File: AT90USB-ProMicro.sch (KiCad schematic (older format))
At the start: 20 parts, among them J1 Conn_01x12, J2 Conn_01x12, J3 Conn_01x03, U1 AT90USB162-16MU, U2 SOT-23 3.3V, X1 8MHz 2520

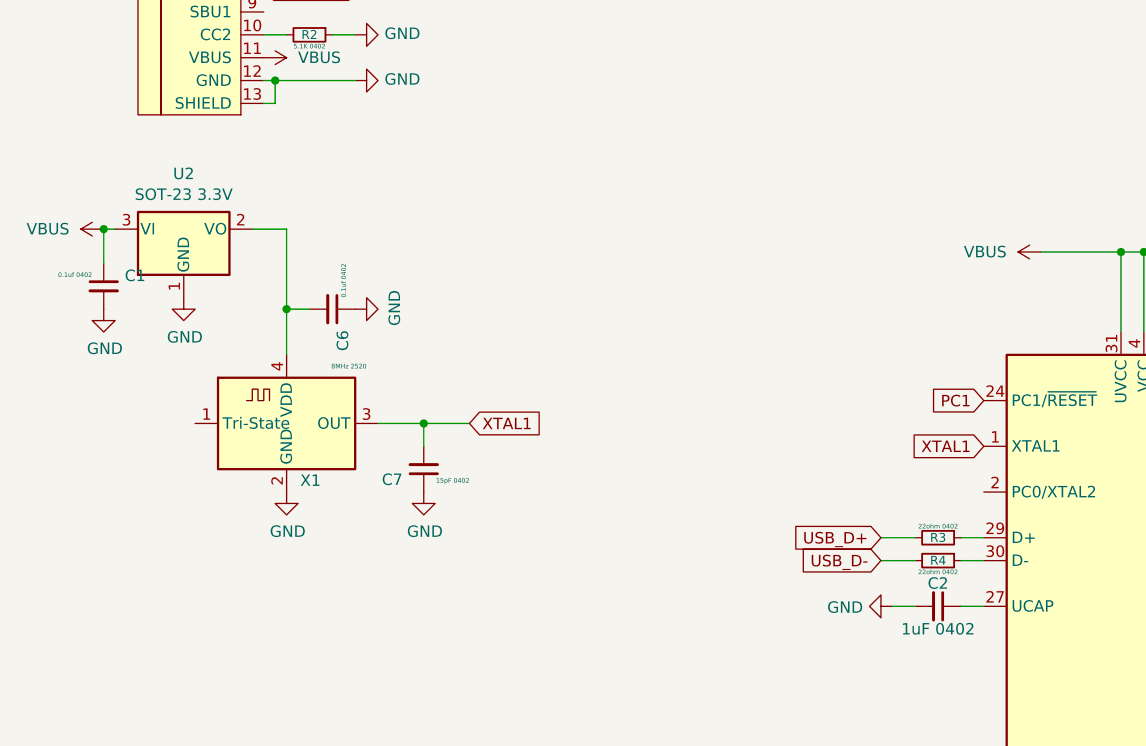
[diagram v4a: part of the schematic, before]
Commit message: changed oscillator for crystal, 3225 gnd on 2 and 4.
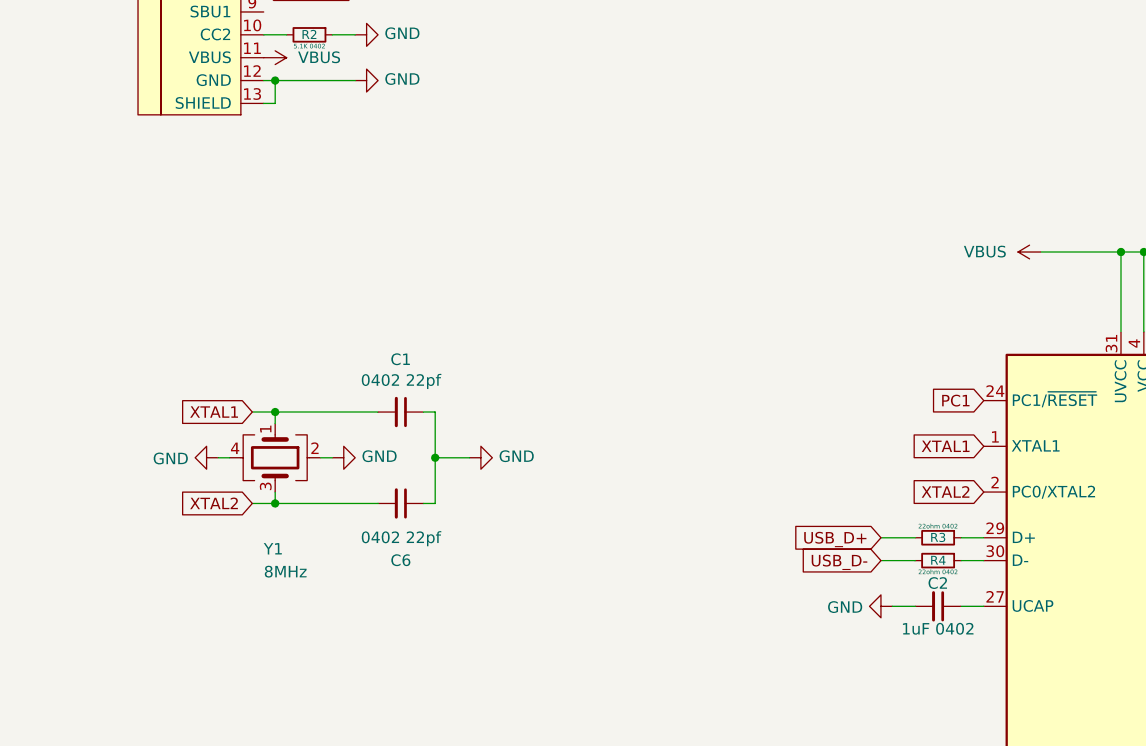
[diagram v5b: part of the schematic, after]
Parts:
- removed C7: 15pF 0402, Capacitor_SMD:C_0402_1005Metric, symbol Device:C_Small
- removed U2: SOT-23 3.3V, Package_TO_SOT_SMD:SOT-23, symbol Regulator_Linear:MCP1703A-3302_SOT23
- removed X1: 8MHz 2520, Oscillator:Oscillator_SMD_ECS_2520MV-xxx-xx-4Pin_2.5x2.0mm, symbol Oscillator:ECS-2520MV-xxx-xx
- added Y1: 8MHz, Crystal:Crystal_SMD_3225-4Pin_3.2x2.5mm, symbol Device:Crystal_GND24
- C1, C6: value 0.1uf 0402 -> 0402 22pf
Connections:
- net GND: now also C1.1, Y1.2, Y1.4; no longer C1.2
- net VBUS: no longer C1.1
- net XTAL1: now also C1.2, Y1.1
- net XTAL2: now reaches U1.2 (PC0/XTAL2)
- net XTAL2: now also C6.2, Y1.3
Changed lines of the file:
@@
 Wire Wire Line
 	4350 5100 4500 5100
-$Comp
-L power:VBUS #PWR0110
-U 1 1 610BDD5E
-P 950 3650
-F 0 "#PWR0110" H 950 3500 50  0001 C CNN
-F 1 "VBUS" V 950 3800 50  0000 L CNN
-F 2 "" H 950 3650 50  0001 C CNN
-F 3 "" H 950 3650 50  0001 C CNN
-	1    950  3650
-	0    -1   -1   0
-$EndComp
 Text GLabel 4800 4600 0    50   Input ~ 0
 XTAL1
-Text GLabel 2550 4500 2    50   Input ~ 0
-XTAL1
-$Comp
-L Device:C_Small C1
-U 1 1 610B5A05
-P 950 3900
-F 0 "C1" H 1042 3946 50  0000 L CNN
-F 1 "0.1uf 0402" H 750 3950 20  0000 L CNN
-F 2 "Capacitor_SMD:C_0402_1005Metric" H 950 3900 50  0001 C CNN
-F 3 "~" H 950 3900 50  0001 C CNN
-	1    950  3900
-	1    0    0    -1
-$EndComp
-Wire Wire Line
-	950  3800 950  3650
-$Comp
-L power:GND #PWR0112
-U 1 1 610B6B7D
-P 950 4000
-F 0 "#PWR0112" H 950 3750 50  0001 C CNN
-F 1 "GND" H 955 3827 50  0000 C CNN
-F 2 "" H 950 4000 50  0001 C CNN
-F 3 "" H 950 4000 50  0001 C CNN
-	1    950  4000
-	1    0    0    -1
-$EndComp
 $Comp
 L Connector_Generic:Conn_01x12 J1
@@
 Connection ~ 5500 6950
 $Comp
-L Oscillator:ECS-2520MV-xxx-xx X1
-U 1 1 611038B7
-P 1750 4500
-F 0 "X1" H 1900 4250 50  0000 R CNN
-F 1 "8MHz 2520" H 2100 4750 20  0000 R CNN
-F 2 "Oscillator:Oscillator_SMD_ECS_2520MV-xxx-xx-4Pin_2.5x2.0mm" H 2200 4150 50  0001 C CNN
-F 3 "https://www.ecsxtal.com/store/pdf/ECS-2520MV.pdf" H 1575 4625 50  0001 C CNN
-	1    1750 4500
-	1    0    0    -1
-$EndComp
-Wire Wire Line
-	950  3650 1000 3650
-Connection ~ 950  3650
-$Comp
-L power:GND #PWR0111
-U 1 1 610BE5C3
-P 1750 4800
-F 0 "#PWR0111" H 1750 4550 50  0001 C CNN
-F 1 "GND" H 1755 4627 50  0000 C CNN
-F 2 "" H 1750 4800 50  0001 C CNN
-F 3 "" H 1750 4800 50  0001 C CNN
-	1    1750 4800
-	1    0    0    -1
-$EndComp
-$Comp
-L power:GND #PWR0114
-U 1 1 61113D49
-P 1300 3950
-F 0 "#PWR0114" H 1300 3700 50  0001 C CNN
-F 1 "GND" H 1305 3777 50  0000 C CNN
-F 2 "" H 1300 3950 50  0001 C CNN
-F 3 "" H 1300 3950 50  0001 C CNN
-	1    1300 3950
-	1    0    0    -1
-$EndComp
-$Comp
-L Regulator_Linear:MCP1703A-3302_SOT23 U2
-U 1 1 611160A9
-P 1300 3650
-F 0 "U2" H 1300 3892 50  0000 C CNN
-F 1 "SOT-23 3.3V" H 1300 3801 50  0000 C CNN
-F 2 "Package_TO_SOT_SMD:SOT-23" H 1300 3850 50  0001 C CNN
-F 3 "http://ww1.microchip.com/downloads/en/DeviceDoc/20005122B.pdf" H 1300 3600 50  0001 C CNN
-	1    1300 3650
-	1    0    0    -1
-$EndComp
-$Comp
 L power:GND #PWR0113
 U 1 1 61140B20
@@
 	0    1    1    0
 $EndComp
-Wire Wire Line
-	1750 4200 1750 4000
-Wire Wire Line
-	1750 3650 1600 3650
+Text GLabel 4800 4800 0    50   Input ~ 0
+XTAL2
+Text GLabel 1600 4850 0    50   Input ~ 0
+XTAL2
+$Comp
+L Device:C_Small C1
+U 1 1 611B395D
+P 2250 4450
+F 0 "C1" V 2021 4450 50  0000 C CNN
+F 1 "0402 22pf" V 2112 4450 50  0000 C CNN
+F 2 "Capacitor_SMD:C_0402_1005Metric" H 2250 4450 50  0001 C CNN
+F 3 "~" H 2250 4450 50  0001 C CNN
+	1    2250 4450
+	0    1    1    0
+$EndComp
 $Comp
 L Device:C_Small C6
-U 1 1 610DB8B7
-P 1950 4000
-F 0 "C6" H 2042 4046 50  0000 L CNN
-F 1 "0.1uf 0402" H 1750 4050 20  0000 L CNN
-F 2 "Capacitor_SMD:C_0402_1005Metric" H 1950 4000 50  0001 C CNN
-F 3 "~" H 1950 4000 50  0001 C CNN
-	1    1950 4000
+U 1 1 611B5404
+P 2250 4850
+F 0 "C6" V 2500 4850 50  0000 C CNN
+F 1 "0402 22pf" V 2400 4850 50  0000 C CNN
+F 2 "Capacitor_SMD:C_0402_1005Metric" H 2250 4850 50  0001 C CNN
+F 3 "~" H 2250 4850 50  0001 C CNN
+	1    2250 4850
 	0    1    1    0
 $EndComp
 $Comp
 L power:GND #PWR02
-U 1 1 610DC063
-P 2050 4000
-F 0 "#PWR02" H 2050 3750 50  0001 C CNN
-F 1 "GND" H 2055 3827 50  0000 C CNN
-F 2 "" H 2050 4000 50  0001 C CNN
-F 3 "" H 2050 4000 50  0001 C CNN
-	1    2050 4000
-	0    -1   -1   0
-$EndComp
-Wire Wire Line
-	1850 4000 1750 4000
-Connection ~ 1750 4000
-Wire Wire Line
-	1750 4000 1750 3650
-$Comp
-L Device:C_Small C7
-U 1 1 610DF85F
-P 2350 4700
-F 0 "C7" H 2442 4746 50  0000 L CNN
-F 1 "15pF 0402" H 2150 4750 20  0000 L CNN
-F 2 "Capacitor_SMD:C_0402_1005Metric" H 2350 4700 50  0001 C CNN
-F 3 "~" H 2350 4700 50  0001 C CNN
-	1    2350 4700
-	-1   0    0    1
-$EndComp
-$Comp
-L power:GND #PWR03
-U 1 1 610DFF21
-P 2350 4800
-F 0 "#PWR03" H 2350 4550 50  0001 C CNN
-F 1 "GND" H 2355 4627 50  0000 C CNN
-F 2 "" H 2350 4800 50  0001 C CNN
-F 3 "" H 2350 4800 50  0001 C CNN
-	1    2350 4800
-	1    0    0    -1
-$EndComp
-Wire Wire Line
-	2150 4500 2350 4500
-Connection ~ 2350 4500
-Wire Wire Line
-	2350 4500 2550 4500
-Wire Wire Line
-	2350 4500 2350 4600
+U 1 1 611B5E53
+P 2550 4650
+F 0 "#PWR02" H 2550 4400 50  0001 C CNN
+F 1 "GND" V 2555 4522 50  0000 R CNN
+F 2 "" H 2550 4650 50  0001 C CNN
+F 3 "" H 2550 4650 50  0001 C CNN
+	1    2550 4650
+	0    -1   -1   0
+$EndComp
+Wire Wire Line
+	2400 4650 2550 4650
+Connection ~ 2400 4650
+Text GLabel 1600 4450 0    50   Input ~ 0
+XTAL1
+Wire Wire Line
+	1600 4450 1700 4450
+Wire Wire Line
+	2350 4450 2400 4450
+Wire Wire Line
+	2400 4450 2400 4650
+Wire Wire Line
+	2350 4850 2400 4850
+Wire Wire Line
+	2400 4650 2400 4850
+Wire Wire Line
+	1600 4850 1700 4850
+Wire Wire Line
+	1700 4850 1700 4800
+Connection ~ 1700 4850
+Wire Wire Line
+	1700 4850 2150 4850
+Wire Wire Line
+	1700 4500 1700 4450
+Connection ~ 1700 4450
+Wire Wire Line
+	1700 4450 2150 4450
+$Comp
+L power:GND #PWR?
+U 1 1 611BF5EC
+P 1950 4650
+F 0 "#PWR?" H 1950 4400 50  0001 C CNN
+F 1 "GND" V 1955 4522 50  0000 R CNN
+F 2 "" H 1950 4650 50  0001 C CNN
+F 3 "" H 1950 4650 50  0001 C CNN
+	1    1950 4650
+	0    -1   -1   0
+$EndComp
+$Comp
+L Device:Crystal_GND24 Y1
+U 1 1 611AA5C7
+P 1700 4650
+F 0 "Y1" V 2100 4600 50  0000 L CNN
+F 1 "8MHz" V 2200 4600 50  0000 L CNN
+F 2 "Crystal:Crystal_SMD_3225-4Pin_3.2x2.5mm" H 1700 4650 50  0001 C CNN
+F 3 "~" H 1700 4650 50  0001 C CNN
+	1    1700 4650
+	0    1    1    0
+$EndComp
+Wire Wire Line
+	1900 4650 1950 4650
+$Comp
+L power:GND #PWR?
+U 1 1 611C4B8D
+P 1450 4650
+F 0 "#PWR?" H 1450 4400 50  0001 C CNN
+F 1 "GND" V 1455 4522 50  0000 R CNN
+F 2 "" H 1450 4650 50  0001 C CNN
+F 3 "" H 1450 4650 50  0001 C CNN
+	1    1450 4650
+	0    1    1    0
+$EndComp
+Wire Wire Line
+	1450 4650 1500 4650
 $EndSCHEMATC
